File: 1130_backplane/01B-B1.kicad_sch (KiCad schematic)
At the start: 86 parts

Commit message: Finish page KR101-KR111
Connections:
- net -B_BIT_CK_2: now reaches J383.b10 (Pin_b10)
- net -B_BIT_CK_2: now also J393.b10 (Pin_b10)
- net -B_BIT_CK_1: now reaches J383.b9 (Pin_b9)
- net -B_BIT_CK_1: now also J393.b9 (Pin_b9)
- net -EVEN_PARITY_1: now reaches J347.a4 (Pin_a4)
- net -EVEN_PARITY_1: now also J412.b4 (Pin_b4)
- net -EVEN_PARITY_2: now reaches J347.a5 (Pin_a5)
- net -EVEN_PARITY_2: now also J418.b4 (Pin_b4)
- net +EVEN_PARITY_1: now reaches J347.b4 (Pin_b4)
- net +EVEN_PARITY_1: now also J412.a12 (Pin_a12)
- net +EVEN_PARITY_2: now reaches J347.b5 (Pin_b5)
- net +EVEN_PARITY_2: now also J418.a12 (Pin_a12)
- net -B_BIT_5_PWR: now reaches J412.a11 (Pin_a11)
- net -B_BIT_0_PWR: now reaches J412.a2 (Pin_a2)
- net -B_BIT_1_PWR: now reaches J412.a4 (Pin_a4)
- net -B_BIT_2_PWR: now reaches J412.a6 (Pin_a6)
- net -B_BIT_3_PWR: now reaches J412.a7 (Pin_a7)
- net -B_BIT_4_PWR: now reaches J412.a9 (Pin_a9)
- net -B_BIT_7_PWR: now reaches J412.b11 (Pin_b11)
- net +CK_BIT_P1: now reaches J412.b5 (Pin_b5)
- net +CK_BIT_P1: now also J350.a11 (Pin_a11)
- net -B_BIT_6_PWR: now reaches J412.b9 (Pin_b9)
- net +CK_BIT_P2: now reaches J348.a11 (Pin_a11)
- net +CK_BIT_P2: now also J418.b5 (Pin_b5)
- net -B_BIT_13_PWR: now reaches J418.a11 (Pin_a11)
- net -B_BIT_8_PWR: now reaches J418.a2 (Pin_a2)
- net -B_BIT_9_PWR: now reaches J418.a4 (Pin_a4)
- net -B_BIT_10_PWR: now reaches J418.a6 (Pin_a6)
- net -B_BIT_11_PWR: now reaches J418.a7 (Pin_a7)
- net -B_BIT_12_PWR: now reaches J418.a9 (Pin_a9)
- net -B_BIT_15_PWR: now reaches J418.b11 (Pin_b11)
- net -B_BIT_14_PWR: now reaches J418.b9 (Pin_b9)
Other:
- note added: "5803022"
- note added: "CABL 01B-A1T2"
- note added: "CABL 01B-C1T4"
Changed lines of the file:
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@@
     (effects (font (size 5 5) (thickness 1) bold) (justify left bottom))
+  )
+  (text "5803022" (at 670.56 292.1 0)
+    (effects (font (size 1.27 1.27)) (justify left bottom))
   )
   (text "C" (at 323.85 26.67 0)
@@
     (effects (font (size 1.27 1.27)) (justify left bottom))
   )
+  (text "5803022" (at 607.06 292.1 0)
+    (effects (font (size 1.27 1.27)) (justify left bottom))
+  )
   (text "A" (at 294.64 24.13 0)
     (effects (font (size 5 5) (thickness 1) bold) (justify left bottom))
@@
     (effects (font (size 1.27 1.27)) (justify left bottom))
   )
+  (text "CABL 01B-C1T4" (at 469.9 24.13 0)
+    (effects (font (size 1.27 1.27)) (justify left bottom))
+  )
   (text "10" (at 21.59 63.5 0)
     (effects (font (size 1.27 1.27)) (justify left bottom))
@@
     (effects (font (size 5 5) (thickness 1) bold) (justify left bottom))
   )
+  (text "CABL 01B-A1T2" (at 393.7 24.13 0)
+    (effects (font (size 1.27 1.27)) (justify left bottom))
+  )
   (text "5803757" (at 353.06 215.9 0)
     (effects (font (size 1.27 1.27)) (justify left bottom))
@@
     (effects (font (size 5 5) (thickness 1) bold) (justify left bottom))
   )
+  (label "-B_BIT_CK_1" (at 407.67 50.8 90)
+    (effects (font (size 1.27 1.27)) (justify left bottom))
+  )
   (label "-M_TO_I_SP_8-15" (at 426.72 165.1 0)
     (effects (font (size 1.27 1.27)) (justify left bottom))
@@
     (effects (font (size 1.27 1.27)) (justify left bottom))
   )
+  (label "+EVEN_PARITY_1" (at 604.52 322.58 180)
+    (effects (font (size 1.27 1.27)) (justify right bottom))
+  )
   (label "GND" (at 688.34 271.78 0)
     (effects (font (size 1.27 1.27)) (justify left bottom))
@@
     (effects (font (size 1.27 1.27)) (justify right bottom))
   )
+  (label "-B_BIT_9_PWR" (at 668.02 302.26 180)
+    (effects (font (size 1.27 1.27)) (justify right bottom))
+  )
   (label "+6V" (at 215.9 127 180)
     (effects (font (size 1.27 1.27)) (justify right bottom))
@@
     (effects (font (size 1.27 1.27)) (justify right bottom))
   )
+  (label "-B_BIT_8_PWR" (at 668.02 297.18 180)
+    (effects (font (size 1.27 1.27)) (justify right bottom))
+  )
   (label "+PHASE_B" (at 477.52 104.14 180)
     (effects (font (size 1.27 1.27)) (justify right bottom))
   )
+  (label "+CK_BIT_P1" (at 617.22 304.8 0)
+    (effects (font (size 1.27 1.27)) (justify left bottom))
+  )
   (label "+I_BIT_13" (at 731.52 208.28 180)
     (effects (font (size 1.27 1.27)) (justify right bottom))
@@
     (effects (font (size 1.27 1.27)) (justify right bottom))
   )
+  (label "+CK_BIT_P2" (at 33.02 243.84 180)
+    (effects (font (size 1.27 1.27)) (justify right bottom))
+  )
   (label "GND" (at 478.79 43.18 90)
     (effects (font (size 1.27 1.27)) (justify left bottom))
@@
     (effects (font (size 1.27 1.27)) (justify left bottom))
   )
+  (label "-B_BIT_10_PWR" (at 668.02 307.34 180)
+    (effects (font (size 1.27 1.27)) (justify right bottom))
+  )
   (label "+3V" (at 434.34 144.78 0)
     (effects (font (size 1.27 1.27)) (justify left bottom))
@@
     (effects (font (size 1.27 1.27)) (justify right bottom))
   )
+  (label "-B_BIT_4_PWR" (at 604.52 314.96 180)
+    (effects (font (size 1.27 1.27)) (justify right bottom))
+  )
   (label "+3V" (at 815.34 182.88 0)
     (effects (font (size 1.27 1.27)) (justify left bottom))
@@
     (effects (font (size 1.27 1.27)) (justify left bottom))
   )
+  (label "-B_BIT_0_PWR" (at 604.52 297.18 180)
+    (effects (font (size 1.27 1.27)) (justify right bottom))
+  )
   (label "GND" (at 243.84 271.78 0)
     (effects (font (size 1.27 1.27)) (justify left bottom))
@@
     (effects (font (size 1.27 1.27)) (justify right bottom))
   )
+  (label "-B_BIT_12_PWR" (at 668.02 314.96 180)
+    (effects (font (size 1.27 1.27)) (justify right bottom))
+  )
   (label "+6V" (at 152.4 317.5 180)
     (effects (font (size 1.27 1.27)) (justify right bottom))
@@
     (effects (font (size 1.27 1.27)) (justify left bottom))
   )
+  (label "-B_BIT_CK_1" (at 483.87 50.8 90)
+    (effects (font (size 1.27 1.27)) (justify left bottom))
+  )
   (label "-RESET_D_REG_SP" (at 45.72 147.32 0)
     (effects (font (size 1.27 1.27)) (justify left bottom))
@@
     (effects (font (size 1.27 1.27)) (justify right bottom))
   )
+  (label "-B_BIT_13_PWR" (at 668.02 320.04 180)
+    (effects (font (size 1.27 1.27)) (justify right bottom))
+  )
   (label "+3V" (at 243.84 220.98 0)
     (effects (font (size 1.27 1.27)) (justify left bottom))
@@
     (effects (font (size 1.27 1.27)) (justify left bottom))
   )
+  (label "-B_BIT_7_PWR" (at 617.22 320.04 0)
+    (effects (font (size 1.27 1.27)) (justify left bottom))
+  )
   (label "+3V" (at 561.34 259.08 0)
     (effects (font (size 1.27 1.27)) (justify left bottom))
@@
     (effects (font (size 1.27 1.27)) (justify left bottom))
   )
+  (label "-B_BIT_5_PWR" (at 604.52 320.04 180)
+    (effects (font (size 1.27 1.27)) (justify right bottom))
+  )
   (label "-U_TO_A_SP_8-15" (at 414.02 233.68 180)
     (effects (font (size 1.27 1.27)) (justify right bottom))
@@
     (effects (font (size 1.27 1.27)) (justify left bottom))
   )
+  (label "-EVEN_PARITY_1" (at 617.22 302.26 0)
+    (effects (font (size 1.27 1.27)) (justify left bottom))
+  )
   (label "+3V" (at 180.34 220.98 0)
     (effects (font (size 1.27 1.27)) (justify left bottom))
@@
     (effects (font (size 1.27 1.27)) (justify right bottom))
   )
+  (label "-B_BIT_3_PWR" (at 604.52 309.88 180)
+    (effects (font (size 1.27 1.27)) (justify right bottom))
+  )
   (label "GND" (at 180.34 233.68 0)
     (effects (font (size 1.27 1.27)) (justify left bottom))
@@
     (effects (font (size 1.27 1.27)) (justify left bottom))
   )
+  (label "+EVEN_PARITY_1" (at 45.72 187.96 0)
+    (effects (font (size 1.27 1.27)) (justify left bottom))
+  )
   (label "-3V" (at 469.9 114.3 180)
     (effects (font (size 1.27 1.27)) (justify right bottom))
@@
     (effects (font (size 1.27 1.27)) (justify right bottom))
   )
+  (label "-B_BIT_2_PWR" (at 604.52 307.34 180)
+    (effects (font (size 1.27 1.27)) (justify right bottom))
+  )
   (label "-3V" (at 660.4 152.4 180)
     (effects (font (size 1.27 1.27)) (justify right bottom))
@@
     (effects (font (size 1.27 1.27)) (justify right bottom))
   )
+  (label "-B_BIT_CK_2" (at 410.21 50.8 90)
+    (effects (font (size 1.27 1.27)) (justify left bottom))
+  )
   (label "-SHIFT_LT_SPD_SAMPLE_A" (at 426.72 226.06 0)
     (effects (font (size 1.27 1.27)) (justify left bottom))
@@
     (effects (font (size 1.27 1.27)) (justify right bottom))
   )
+  (label "-B_BIT_15_PWR" (at 680.72 320.04 0)
+    (effects (font (size 1.27 1.27)) (justify left bottom))
+  )
   (label "-3V" (at 787.4 266.7 180)
     (effects (font (size 1.27 1.27)) (justify right bottom))
@@
     (effects (font (size 1.27 1.27)) (justify right bottom))
   )
+  (label "-EVEN_PARITY_2" (at 33.02 190.5 180)
+    (effects (font (size 1.27 1.27)) (justify right bottom))
+  )
   (label "-IO_BIT_0" (at 731.52 218.44 180)
     (effects (font (size 1.27 1.27)) (justify right bottom))
@@
     (effects (font (size 1.27 1.27)) (justify left bottom))
   )
+  (label "-B_BIT_6_PWR" (at 617.22 314.96 0)
+    (effects (font (size 1.27 1.27)) (justify left bottom))
+  )
   (label "-SHIFT_LEFT_A_SP_8-15" (at 426.72 223.52 0)
     (effects (font (size 1.27 1.27)) (justify left bottom))
@@
     (effects (font (size 1.27 1.27)) (justify left bottom))
   )
+  (label "+CK_BIT_P2" (at 680.72 304.8 0)
+    (effects (font (size 1.27 1.27)) (justify left bottom))
+  )
   (label "GND" (at 53.34 271.78 0)
     (effects (font (size 1.27 1.27)) (justify left bottom))
@@
     (effects (font (size 1.27 1.27)) (justify left bottom))
   )
+  (label "-B_BIT_11_PWR" (at 668.02 309.88 180)
+    (effects (font (size 1.27 1.27)) (justify right bottom))
+  )
   (label "-3V" (at 596.9 152.4 180)
     (effects (font (size 1.27 1.27)) (justify right bottom))
@@
     (effects (font (size 1.27 1.27)) (justify left bottom))
   )
+  (label "-EVEN_PARITY_2" (at 680.72 302.26 0)
+    (effects (font (size 1.27 1.27)) (justify left bottom))
+  )
   (label "-3V" (at 723.9 304.8 180)
     (effects (font (size 1.27 1.27)) (justify right bottom))
@@
     (effects (font (size 1.27 1.27)) (justify right bottom))
   )
+  (label "+EVEN_PARITY_2" (at 668.02 322.58 180)
+    (effects (font (size 1.27 1.27)) (justify right bottom))
+  )
   (label "GND" (at 815.34 157.48 0)
     (effects (font (size 1.27 1.27)) (justify left bottom))
@@
     (effects (font (size 1.27 1.27)) (justify left bottom))
   )
+  (label "-EVEN_PARITY_1" (at 33.02 187.96 180)
+    (effects (font (size 1.27 1.27)) (justify right bottom))
+  )
   (label "GND" (at 434.34 119.38 0)
     (effects (font (size 1.27 1.27)) (justify left bottom))
@@
     (effects (font (size 1.27 1.27)) (justify left bottom))
   )
+  (label "-B_BIT_CK_2" (at 486.41 50.8 90)
+    (effects (font (size 1.27 1.27)) (justify left bottom))
+  )
   (label "+3V" (at 624.84 144.78 0)
     (effects (font (size 1.27 1.27)) (justify left bottom))
@@
     (effects (font (size 1.27 1.27)) (justify right bottom))
   )
+  (label "-B_BIT_14_PWR" (at 680.72 314.96 0)
+    (effects (font (size 1.27 1.27)) (justify left bottom))
+  )
+  (label "+EVEN_PARITY_2" (at 45.72 190.5 0)
+    (effects (font (size 1.27 1.27)) (justify left bottom))
+  )
   (label "-3V" (at 660.4 190.5 180)
     (effects (font (size 1.27 1.27)) (justify right bottom))
@@
     (effects (font (size 1.27 1.27)) (justify right bottom))
   )
+  (label "+CK_BIT_P1" (at 33.02 320.04 180)
+    (effects (font (size 1.27 1.27)) (justify right bottom))
+  )
   (label "-INC_IAR_SAMPLE" (at 414.02 238.76 180)
     (effects (font (size 1.27 1.27)) (justify right bottom))
@@
     (effects (font (size 1.27 1.27)) (justify right bottom))
   )
+  (label "-B_BIT_1_PWR" (at 604.52 302.26 180)
+    (effects (font (size 1.27 1.27)) (justify right bottom))
+  )

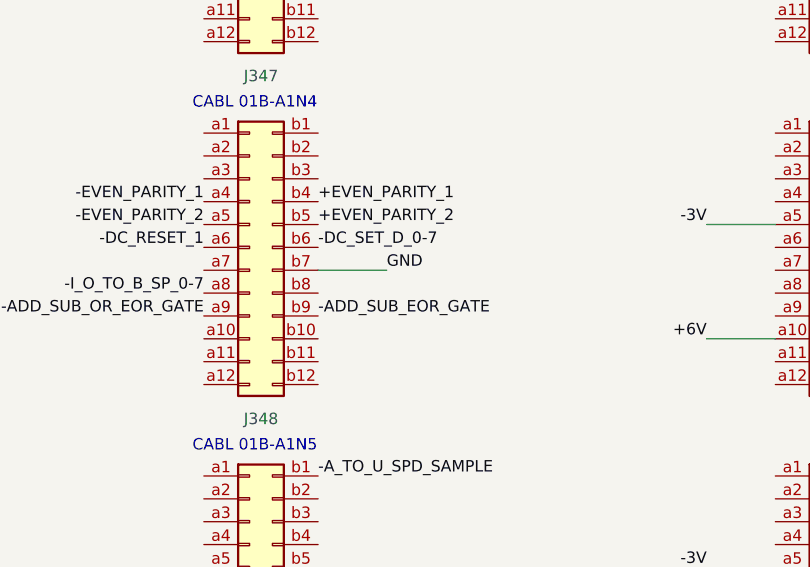
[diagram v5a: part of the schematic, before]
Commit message: Finish page KT101-KT131
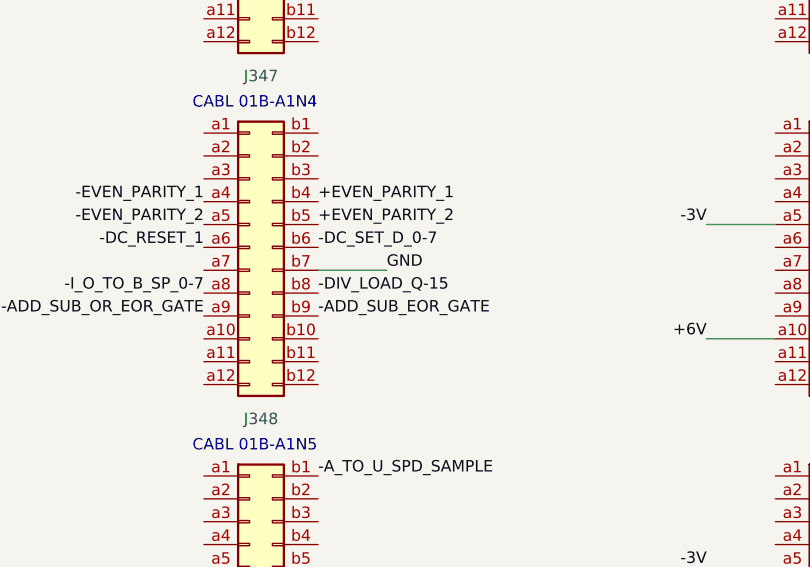
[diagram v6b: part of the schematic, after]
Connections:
- net -DIV_LOAD_Q-15: now reaches J347.b8 (Pin_b8)
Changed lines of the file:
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@@
     (effects (font (size 1.27 1.27)) (justify right bottom))
+  )
+  (label "-DIV_LOAD_Q-15" (at 45.72 198.12 0)
+    (effects (font (size 1.27 1.27)) (justify left bottom))
   )
   (label "-IO_BIT_12" (at 731.52 236.22 180)

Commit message: Finish page KT201
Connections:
- net -ADD_GATE_A: now reaches J347.a10 (Pin_a10)
- net +ACC_BIT_15_SHIFT_LT_ENTRY: now reaches J347.a12 (Pin_a12)
- net -SUB_GATE: now reaches J347.b10 (Pin_b10)
- net -ACC_BIT_15_SHIFT_LT_ENTRY: now reaches J347.b12 (Pin_b12)
- net -ADD_GATE_B: now reaches J348.b5 (Pin_b5)
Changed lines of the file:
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@@
     (effects (font (size 1.27 1.27)) (justify right bottom))
+  )
+  (label "-ADD_GATE_B" (at 45.72 228.6 0)
+    (effects (font (size 1.27 1.27)) (justify left bottom))
   )
   (label "+3V" (at 497.84 259.08 0)
@@
     (effects (font (size 1.27 1.27)) (justify left bottom))
   )
+  (label "-ADD_GATE_A" (at 33.02 203.2 180)
+    (effects (font (size 1.27 1.27)) (justify right bottom))
+  )
   (label "-EXCHANGE_A_AND_Q_SP_0-3" (at 350.52 182.88 180)
     (effects (font (size 1.27 1.27)) (justify right bottom))
@@
     (effects (font (size 1.27 1.27)) (justify right bottom))
   )
+  (label "-SUB_GATE" (at 45.72 203.2 0)
+    (effects (font (size 1.27 1.27)) (justify left bottom))
+  )
   (label "-PHASE_A_SP_B" (at 363.22 198.12 0)
     (effects (font (size 1.27 1.27)) (justify left bottom))
@@
     (effects (font (size 1.27 1.27)) (justify left bottom))
   )
+  (label "+ACC_BIT_15_SHIFT_LT_ENTRY" (at 33.02 208.28 180)
+    (effects (font (size 1.27 1.27)) (justify right bottom))
+  )
   (label "+3V" (at 688.34 182.88 0)
     (effects (font (size 1.27 1.27)) (justify left bottom))
@@
     (effects (font (size 1.27 1.27)) (justify right bottom))
   )
+  (label "-ACC_BIT_15_SHIFT_LT_ENTRY" (at 45.72 208.28 0)
+    (effects (font (size 1.27 1.27)) (justify left bottom))
+  )
   (label "-3V" (at 596.9 114.3 180)

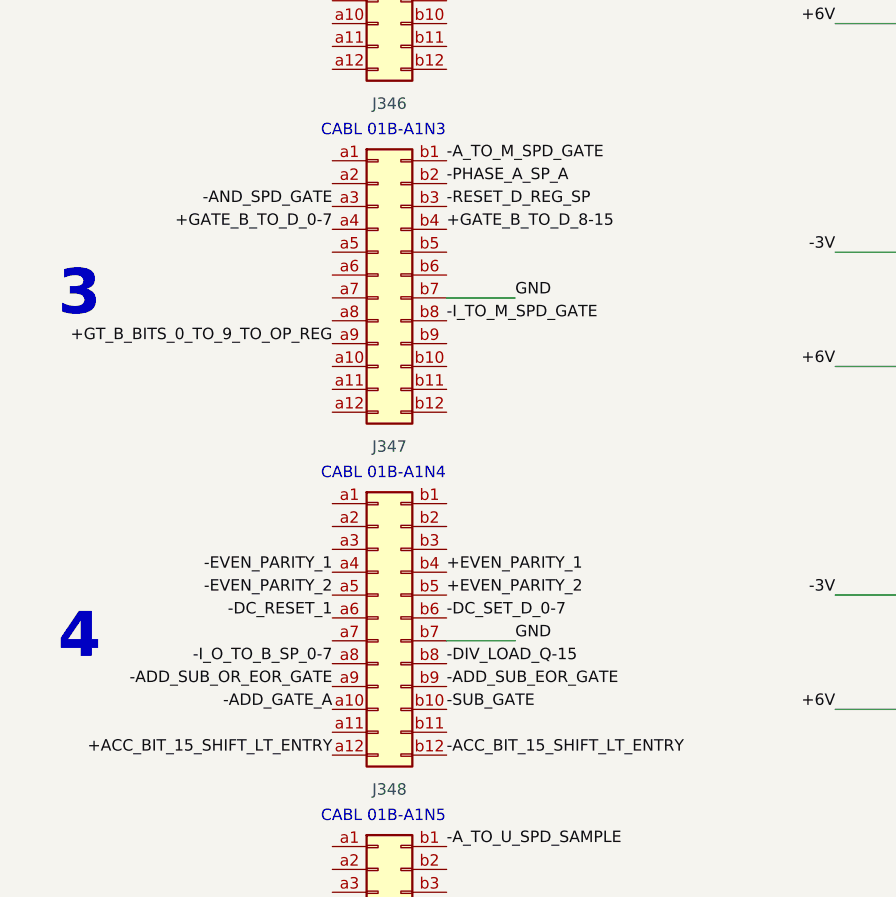
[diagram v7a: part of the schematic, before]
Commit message: Finish page KT301-KT331
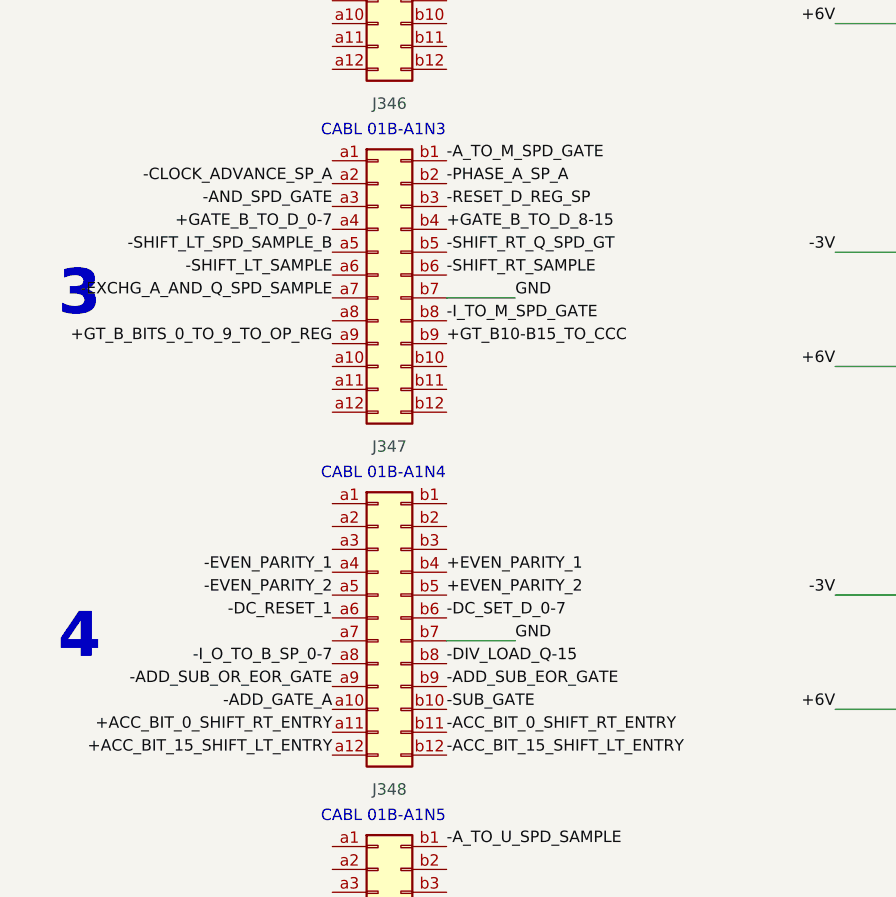
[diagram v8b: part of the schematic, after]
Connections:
- net -CLOCK_ADVANCE_SP_A: now also J346.a2 (Pin_a2)
- net -EXCHG_A_AND_Q_SPD_SAMPLE: now also J346.a7 (Pin_a7)
- net -SHIFT_LT_SAMPLE: now also J346.a6 (Pin_a6)
- net -SHIFT_LT_SPD_SAMPLE_B: now also J346.a5 (Pin_a5)
- net -SHIFT_RT_Q_SPD_GT: now also J346.b5 (Pin_b5)
- net -SHIFT_RT_SAMPLE: now also J346.b6 (Pin_b6)
- net +ACC_BIT_0_SHIFT_RT_ENTRY: now reaches J347.a11 (Pin_a11)
- net -ACC_BIT_0_SHIFT_RT_ENTRY: now reaches J347.b11 (Pin_b11)
- net +GT_B10-B15_TO_CCC: now reaches J346.b9 (Pin_b9)
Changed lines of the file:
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@@
     (effects (font (size 1.27 1.27)) (justify right bottom))
+  )
+  (label "+GT_B10-B15_TO_CCC" (at 45.72 162.56 0)
+    (effects (font (size 1.27 1.27)) (justify left bottom))
   )
   (label "-B_BIT_9_PWR" (at 668.02 302.26 180)
@@
     (effects (font (size 1.27 1.27)) (justify left bottom))
   )
+  (label "-CLOCK_ADVANCE_SP_A" (at 33.02 144.78 180)
+    (effects (font (size 1.27 1.27)) (justify right bottom))
+  )
   (label "KM201_AD4" (at 223.52 309.88 180)
     (effects (font (size 1.27 1.27)) (justify right bottom))
@@
     (effects (font (size 1.27 1.27)) (justify left bottom))
   )
+  (label "+ACC_BIT_0_SHIFT_RT_ENTRY" (at 33.02 205.74 180)
+    (effects (font (size 1.27 1.27)) (justify right bottom))
+  )
   (label "+6V" (at 152.4 279.4 180)
     (effects (font (size 1.27 1.27)) (justify right bottom))
@@
     (effects (font (size 1.27 1.27)) (justify left bottom))
   )
+  (label "-SHIFT_RT_SAMPLE" (at 45.72 154.94 0)
+    (effects (font (size 1.27 1.27)) (justify left bottom))
+  )
   (label "+GATE_B_TO_D_0-7" (at 33.02 149.86 180)
     (effects (font (size 1.27 1.27)) (justify right bottom))
@@
     (effects (font (size 1.27 1.27)) (justify right bottom))
   )
+  (label "-SHIFT_LT_SPD_SAMPLE_B" (at 33.02 152.4 180)
+    (effects (font (size 1.27 1.27)) (justify right bottom))
+  )
   (label "-RESET_D_REG_SP" (at 490.22 104.14 0)
     (effects (font (size 1.27 1.27)) (justify left bottom))
@@
     (effects (font (size 1.27 1.27)) (justify left bottom))
   )
+  (label "-SHIFT_RT_Q_SPD_GT" (at 45.72 152.4 0)
+    (effects (font (size 1.27 1.27)) (justify left bottom))
+  )
   (label "-3V" (at 723.9 228.6 180)
     (effects (font (size 1.27 1.27)) (justify right bottom))
@@
     (effects (font (size 1.27 1.27)) (justify right bottom))
   )
+  (label "-ACC_BIT_0_SHIFT_RT_ENTRY" (at 45.72 205.74 0)
+    (effects (font (size 1.27 1.27)) (justify left bottom))
+  )
   (label "-3V" (at 723.9 152.4 180)
     (effects (font (size 1.27 1.27)) (justify right bottom))
@@
     (effects (font (size 1.27 1.27)) (justify left bottom))
   )
+  (label "-EXCHG_A_AND_Q_SPD_SAMPLE" (at 33.02 157.48 180)
+    (effects (font (size 1.27 1.27)) (justify right bottom))
+  )
   (label "-SHIFT_LEFT_Q_SP_0-7" (at 363.22 185.42 0)
     (effects (font (size 1.27 1.27)) (justify left bottom))
@@
     (effects (font (size 1.27 1.27)) (justify left bottom))
   )
+  (label "-SHIFT_LT_SAMPLE" (at 33.02 154.94 180)
+    (effects (font (size 1.27 1.27)) (justify right bottom))
+  )
   (label "-IO_BIT_14" (at 795.02 238.76 180)
